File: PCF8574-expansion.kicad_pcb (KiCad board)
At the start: 2 copper layers, 69 x 36 mm, 20 parts, among them J1 I2C, J2 LED_1, J3 LED_2, J4 LED_3, J5 LED_4, J6 Power, J7 I2C, J8 Power, U1 PCF8574

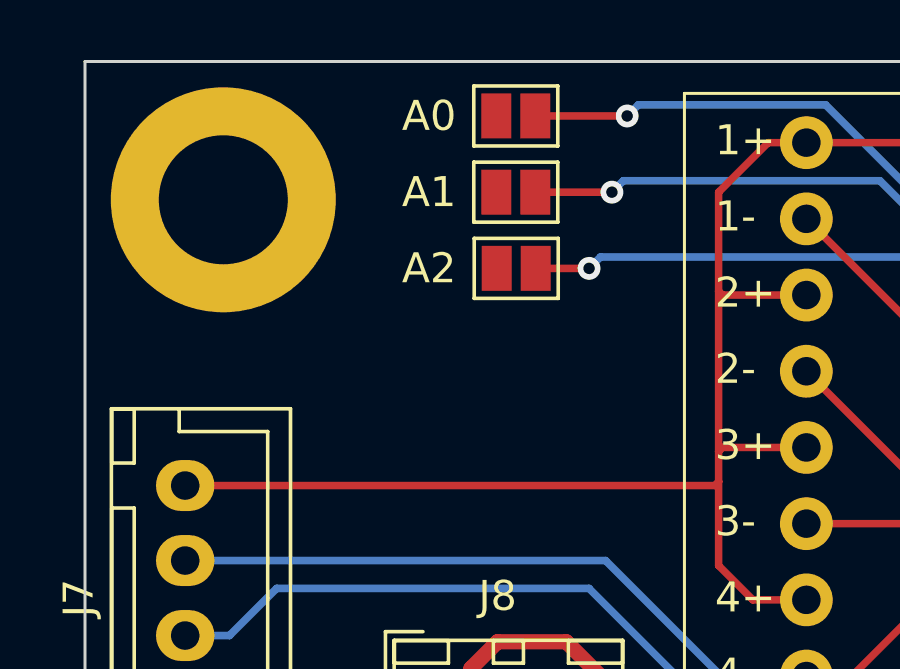
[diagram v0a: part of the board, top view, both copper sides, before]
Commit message: Added adress pullups
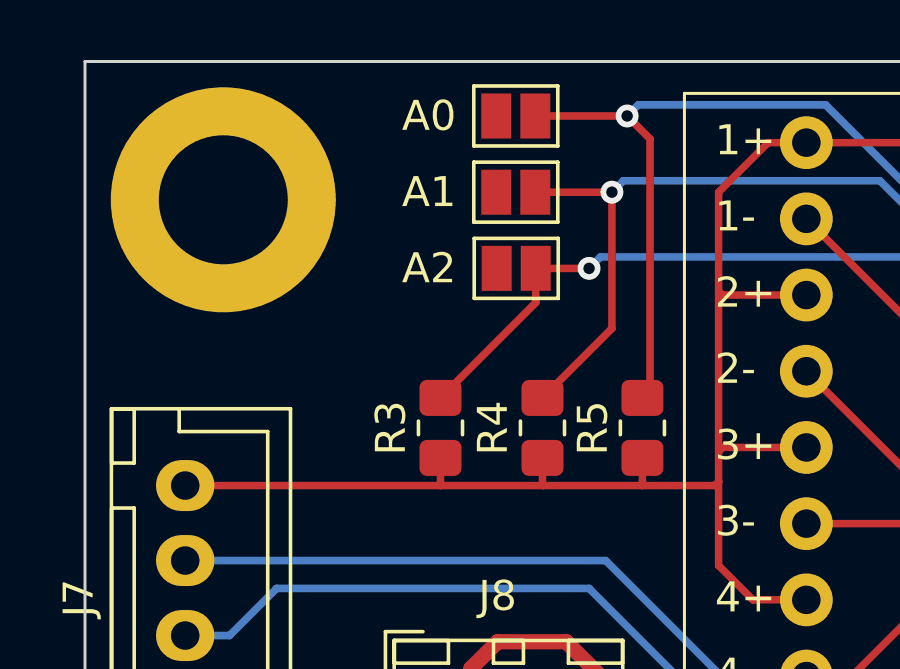
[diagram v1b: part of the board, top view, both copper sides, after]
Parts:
- added R3: 10K, Resistor_SMD:R_0805_2012Metric_Pad1.20x1.40mm_HandSolder, F.Cu at (61.8, 62.2)
- added R4: 10K, Resistor_SMD:R_0805_2012Metric_Pad1.20x1.40mm_HandSolder, F.Cu at (65.2, 62.2)
- added R5: 10K, Resistor_SMD:R_0805_2012Metric_Pad1.20x1.40mm_HandSolder, F.Cu at (68.6, 62.2)
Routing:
- net Net-(JP1-B): track 24.1 -> 33.9 mm
- net Net-(JP2-B): track 23.9 -> 31.7 mm
- net Net-(JP3-B): track 23.7 -> 29.3 mm
- net +VSW: track 99.3 -> 102.1 mm
